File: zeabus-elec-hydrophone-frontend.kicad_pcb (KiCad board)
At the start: 4 copper layers, 53.3 x 68.6 mm, 153 parts, among them CN1 EPS.00.250.NTN, CN2 EPS.00.250.NTN, CN3 EPS.00.250.NTN, CN4 EPS.00.250.NTN, J1 Conn_R1, J10 TEST_1P, J11 TEST_1P, J12 TEST_1P, J13 TEST_1P, J14 TEST_1P, J15 TEST_1P, J16 TEST_1P, J17 TEST_1P, J18 TEST_1P, J2 Conn_L1, J3 Conn_R2, J4 Conn_L2, J5 TEST_1P, J6 TEST_1P, J7 TEST_1P, J8 TEST_1P, J9 TEST_1P, U1 AD8334ACPZ, U2 TLV73311PDBVT, U3 MAX5387LAUD+T, U4 OPA2365, U5 OPA2365

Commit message: First released
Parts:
- added REF**: 1pin, Connectors:1pin, F.Cu at (175.4, 78.9)
- added REF**: 1pin, Connectors:1pin, F.Cu at (129.9, 79.0)
- C39, C40, C41, C42, C43, C44, C45, C46, C47, C49, C50, C51, C52, C53, C54, R21, R22, R23, R24, R25, R26, R27, R28, R29, R30, R31, R32, R33, R34, R35, R36, R37, R38, R39, R40, R41, R42, R43, R44, R45, R46, R47, R48, R49, R50, U4, U5: moved to B.Cu
- C48: footprint Capacitors_SMD:C_1206_HandSoldering -> Capacitors_SMD:C_1210_HandSoldering; moved to B.Cu
- moved C50 78.2 mm to (169.5, 97.5), turned to 180 degrees
- moved C26 74.1 mm to (164.5, 94.0), turned to 180 degrees
- moved C52 73.6 mm to (165.0, 109.5), turned to 180 degrees
- moved L20 71.1 mm to (159.0, 84.6)
- moved C38 68.6 mm to (162.6, 100.9), turned to 90 degrees
- moved C54 68.2 mm to (165.2, 97.5)
- moved C27 67.0 mm to (159.6, 125.9)
- moved C25 65.9 mm to (164.1, 100.8), turned to 90 degrees
- moved L13 65.6 mm to (159.0, 87.9)
- moved C37 64.4 mm to (164.1, 105.2), turned to 270 degrees
- moved C36 63.5 mm to (171.3, 124.3), turned to 180 degrees
- moved C42 63.4 mm to (165.0, 107.8), turned to 180 degrees
- moved L16 63.1 mm to (144.3, 91.1), turned to 180 degrees
- moved L17 63.1 mm to (154.2, 84.6)
- moved C35 63.1 mm to (171.3, 125.9)
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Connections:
- U2 pad 1: +3.3VA -> +3V3
- U2 pad 3: +3.3VA -> +3V3
- U4 pad 5: Net-(R22-Pad1) -> Net-(R37-Pad1)
- U4 pad 6: Net-(R32-Pad1) -> Net-(R47-Pad1)
- U4 pad 7: Net-(R28-Pad2) -> Net-(R43-Pad2)
- U5 pad 1: Net-(R43-Pad2) -> Net-(R28-Pad2)
- U5 pad 2: Net-(R47-Pad1) -> Net-(R32-Pad1)
- U5 pad 3: Net-(R37-Pad1) -> Net-(R22-Pad1)
- U5 pad 4: Net-(U5-Pad4) -> GNDA
- U5 pad 8: Net-(U5-Pad8) -> +3V3
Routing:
- net +3V3: track 0.00 -> 94.6 mm, vias 0 -> 1
- net VA_REF: track 0.00 -> 72.8 mm
- net /ADC3: track 0.00 -> 49.8 mm
- net +5V: track 0.00 -> 43.0 mm, vias 0 -> 7
- net /LNA Gain Control/GAIN12: track 0.00 -> 42.8 mm, vias 0 -> 2
- net /LNA/LNA1RN: track 0.00 -> 41.5 mm
- net /ADC2: track 0.00 -> 40.0 mm
- net /LNA/LNA2RP: track 0.00 -> 39.7 mm
- net /ADC0: track 0.00 -> 35.0 mm
- net /ADC1: track 0.00 -> 33.7 mm
- net /LNA/INH3: track 0.00 -> 33.5 mm
- net /LNA/INH4: track 0.00 -> 33.1 mm
- net /LNA/LNA2LN: track 0.00 -> 32.9 mm
- net /LNA/LNA1LN: track 0.00 -> 32.2 mm
- net /LNA/LNA1LP: track 0.00 -> 30.1 mm
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- added copper zone on In2.Cu, net +5V
- added copper zone on B.Cu, net GNDA
- added copper zone on F.Cu, net GNDA
- added copper zone on In1.Cu, net GNDA
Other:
- net class Default: clearance 0.2 -> 0.127; trace_width 0.25 -> 0.127; via_dia 0.6 -> 0.5588; via_drill 0.4 -> 0.3048
- rule trace_clearance: 0.2 -> 0.127
- rule trace_min: 0.2 -> 0.127
- rule via_min_drill: 0.3 -> 0.3048
- rule via_min_size: 0.4 -> 0.5588

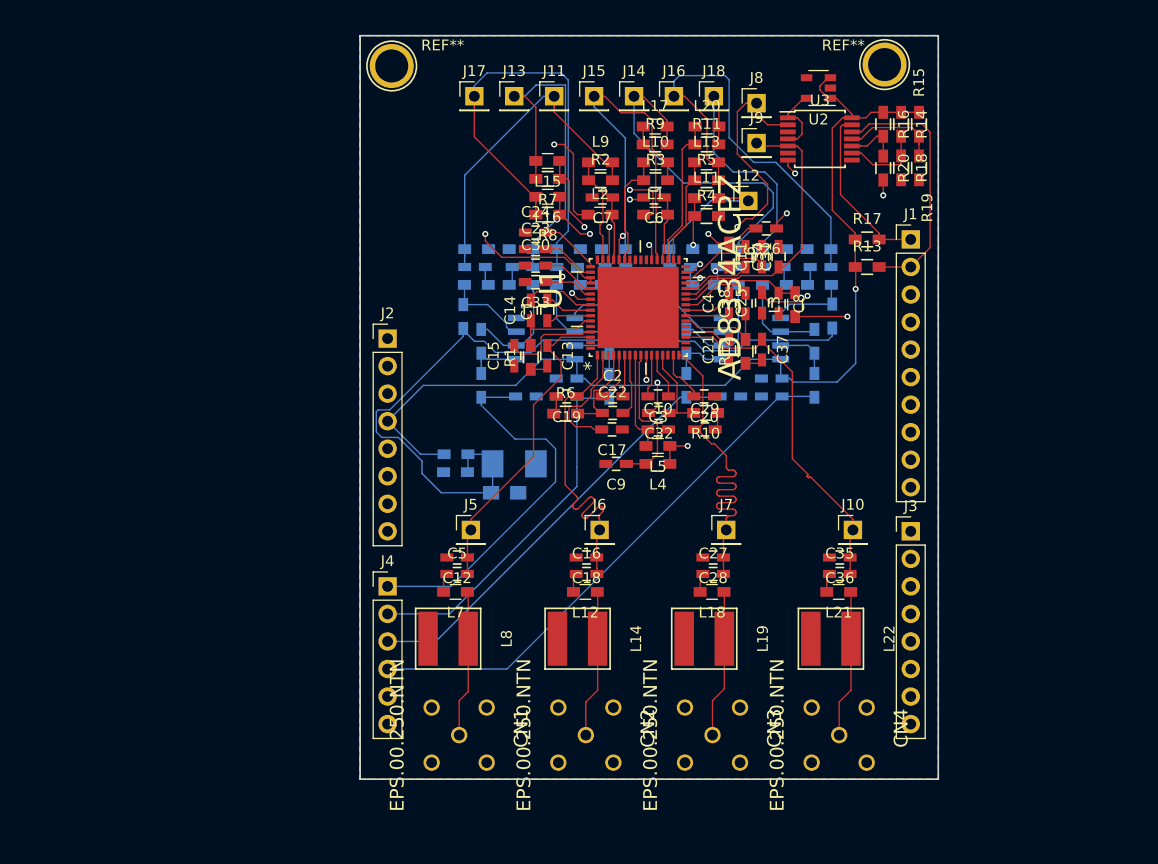
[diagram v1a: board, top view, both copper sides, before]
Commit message: edit layout and silkscreen
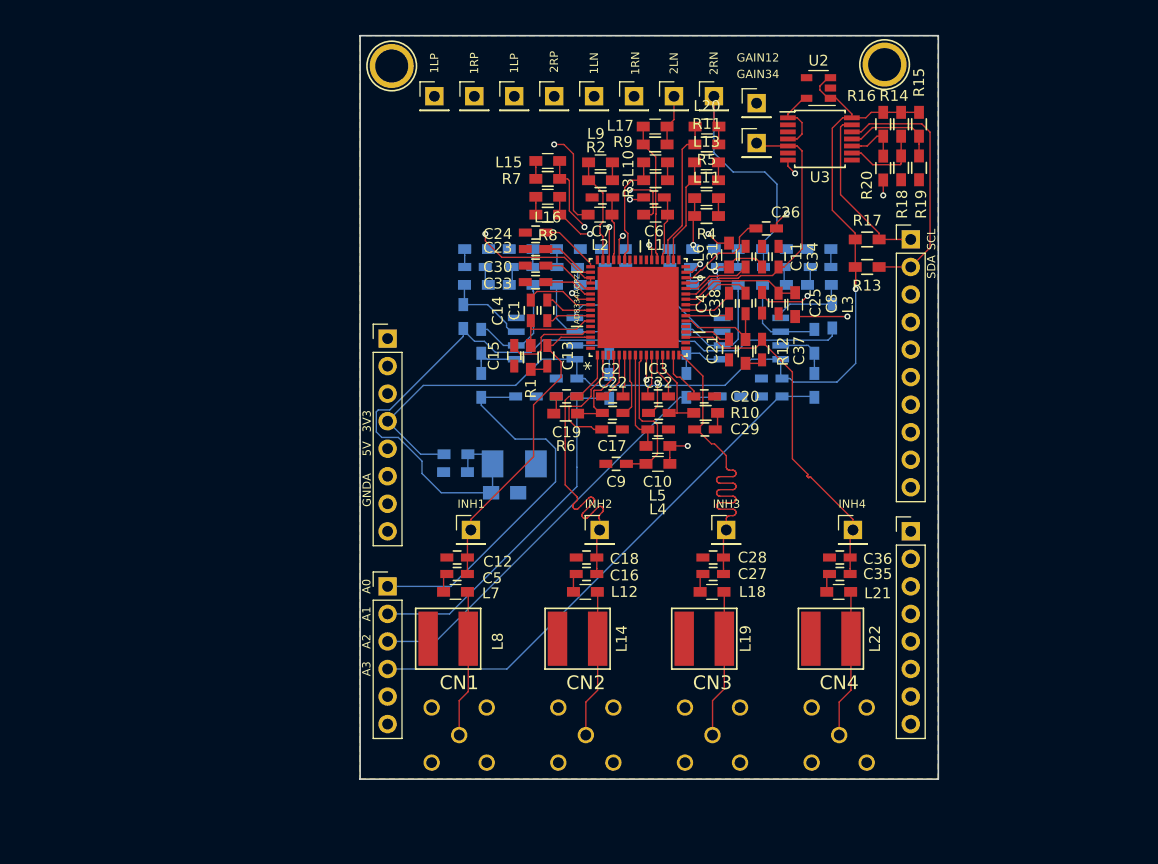
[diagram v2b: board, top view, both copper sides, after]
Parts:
- moved J12 23.6 mm to (141.2, 81.8)
- moved J17 14.7 mm to (152.3, 81.8)
- moved J11 11.0 mm to (133.9, 81.8)
- moved J15 11.0 mm to (137.5, 81.8)
- moved J16 11.0 mm to (144.9, 81.8)
- moved J13 7.37 mm to (148.6, 81.8)
- moved J14 3.68 mm to (156.0, 81.8)
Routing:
- net /LNA Gain Control/GAIN12: track 42.8 -> 4.58 mm, vias 2 -> 0
- net /LNA/LNA1RN: track 41.5 -> 3.47 mm
- net /LNA/LNA2RP: track 39.7 -> 3.30 mm
- net /LNA/LNA1LN: track 32.2 -> 3.31 mm
- net /LNA/LNA1LP: track 30.1 -> 3.30 mm
- net /LNA/LNA2LN: track 32.9 -> 6.37 mm
- net /LNA/LNA1RP: track 29.5 -> 3.47 mm
- net /LNA/LNA2LP: track 15.7 -> 3.34 mm
- net /LNA/LNA2RN: track 25.1 -> 25.8 mm
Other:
- board text added: "1LN"
- board text added: "1LP"
- board text added: "1RN"
- board text added: "1RP"
- board text added: "2LN"
- board text added: "2RN"
- board text added: "2RP"
- board text added: "3V3"
- board text added: "5V"
- board text added: "A0"
- board text added: "A1"
- board text added: "A2"
- board text added: "A3"
- board text added: "GAIN12"
- board text added: "GAIN34"
- board text added: "GNDA"
- board text added: "INH1"
- board text added: "INH2"
- board text added: "INH3"
- board text added: "INH4"
- board text added: "SCL"
- board text added: "SDA"

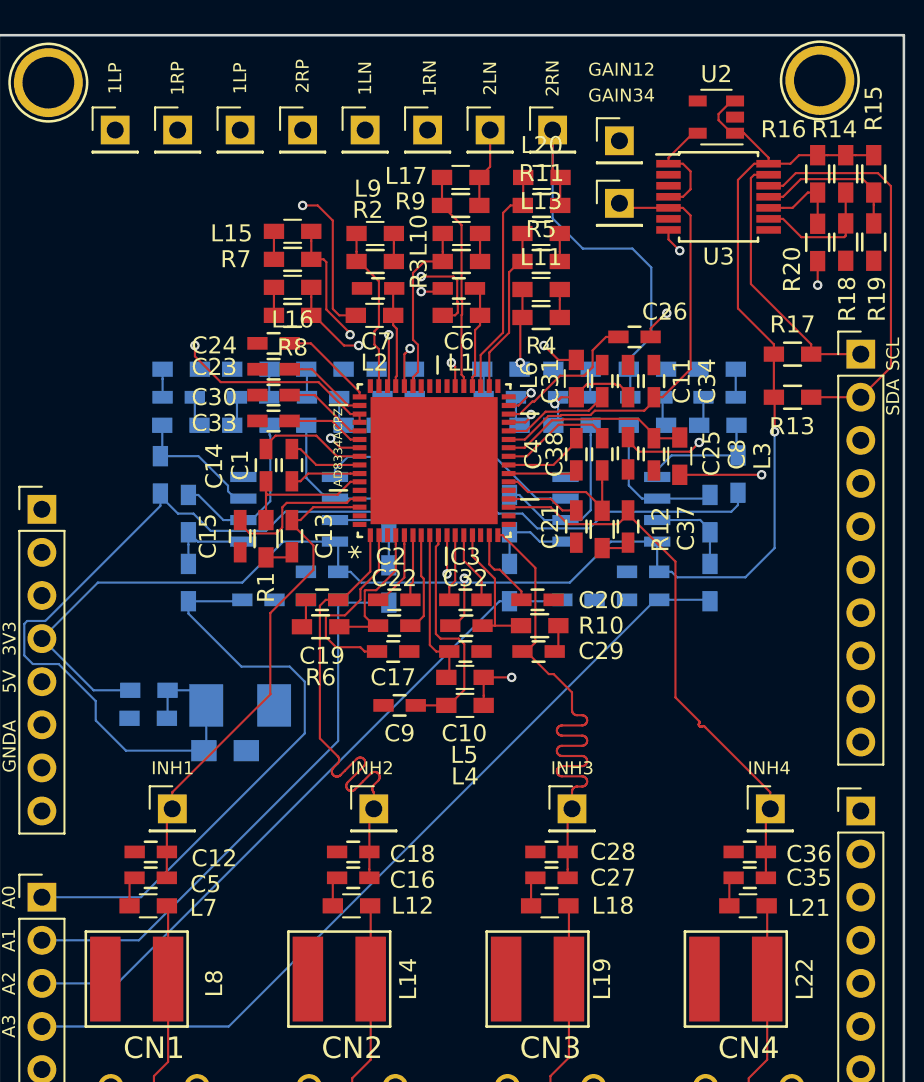
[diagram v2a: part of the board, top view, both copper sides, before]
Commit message: Finished the PCB plus adding some stitching vias
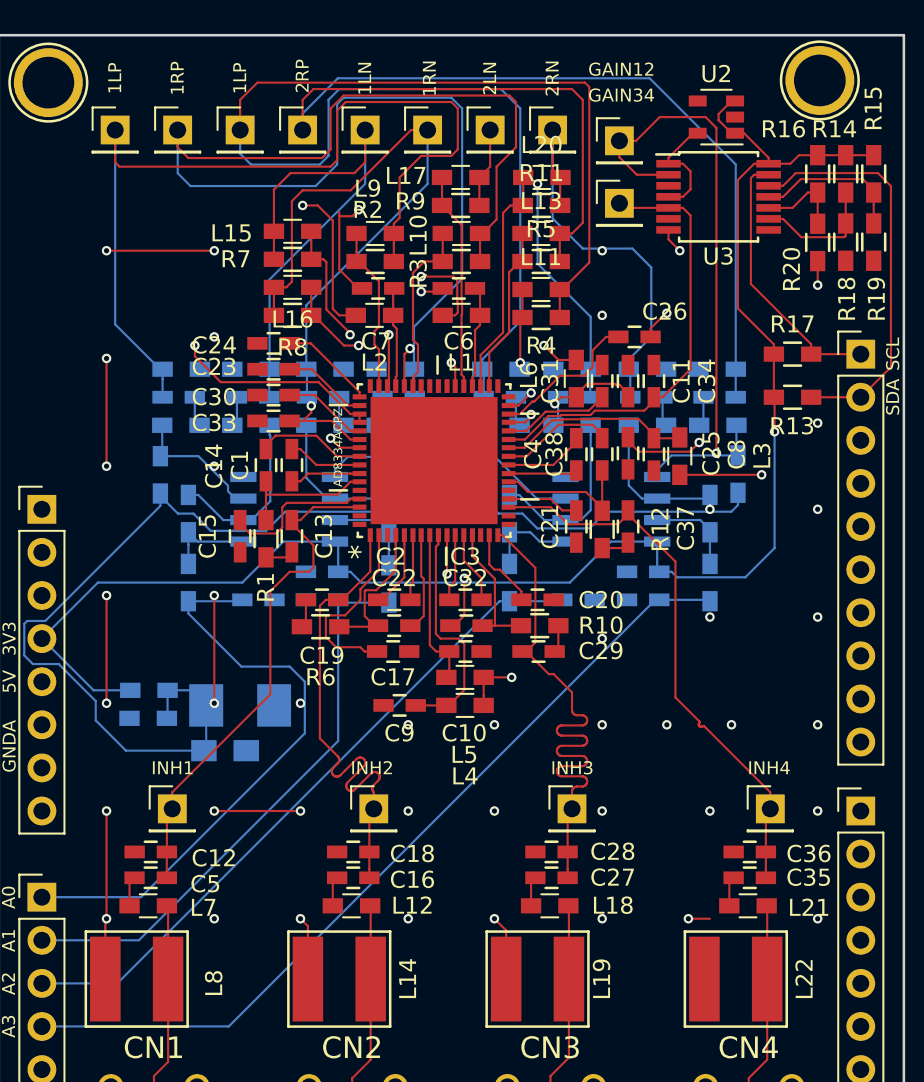
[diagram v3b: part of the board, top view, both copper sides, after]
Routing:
- net GNDA: track 6.10 -> 100.0 mm, vias 4 -> 19
- net /LNA/LNA2LP: track 3.34 -> 77.7 mm
- net /LNA/LNA1RP: track 3.47 -> 77.2 mm
- net /LNA/LNA2RP: track 3.30 -> 72.5 mm
- net /LNA Gain Control/GAIN12: track 4.58 -> 63.5 mm, vias 0 -> 2
- net /LNA/LNA1LP: track 3.30 -> 54.4 mm
- net /LNA/LNA1RN: track 3.47 -> 36.2 mm
- net /LNA/LNA1LN: track 3.31 -> 30.1 mm
- net /LNA/LNA2LN: track 6.37 -> 22.9 mm, vias 0 -> 1
- net (no net): track 0.00 -> 6.35 mm, vias 0 -> 27
- net /LNA/INH1: track 29.5 -> 30.2 mm

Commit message: add gerber file and sent to pcbway
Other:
- board text added: "ZEABUS Hydrophone Sensor Front End REV 1.0"
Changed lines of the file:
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@@
     (links 291)
     (no_connects 0)
-    (area 126.293952 76.124999 181.141286 154.876501)
+    (area 126.293952 68.547 190.273715 154.876501)
     (thickness 1.6)
-    (drawings 27)
+    (drawings 30)
     (tracks 1128)
     (zones 0)
@@
     (visible_elements 7FFFFFFF)
     (pcbplotparams
-      (layerselection 0x00030_80000001)
-      (usegerberextensions false)
+      (layerselection 0x030fc_80000007)
+      (usegerberextensions true)
       (excludeedgelayer true)
       (linewidth 0.100000)
@@
       (plotinvisibletext false)
       (padsonsilk false)
-      (subtractmaskfromsilk false)
+      (subtractmaskfromsilk true)
       (outputformat 1)
       (mirror false)
-      (drillshape 1)
+      (drillshape 0)
       (scaleselection 1)
-      (outputdirectory ""))
+      (outputdirectory plot/))
   )
   (net 0 "")
@@
       (net 12 GNDA))
   )
+  (gr_text "ZEABUS Hydrophone \nSensor Front End \nREV 1.0" (at 130.302 93.091 270) (layer F.SilkS)
+    (effects (font (size 0.762 0.762) (thickness 0.127)))
+  )
+  (dimension 68.58 (width 0.3) (layer Margin)
+    (gr_text "2.7000 in" (at 184.738 110.49 270) (layer Margin)
+      (effects (font (size 1.5 1.5) (thickness 0.3)))
+    )
+    (feature1 (pts (xy 180.34 144.78) (xy 186.088 144.78)))
+    (feature2 (pts (xy 180.34 76.2) (xy 186.088 76.2)))
+    (crossbar (pts (xy 183.388 76.2) (xy 183.388 144.78)))
+    (arrow1a (pts (xy 183.388 144.78) (xy 182.801579 143.653496)))
+    (arrow1b (pts (xy 183.388 144.78) (xy 183.974421 143.653496)))
+    (arrow2a (pts (xy 183.388 76.2) (xy 182.801579 77.326504)))
+    (arrow2b (pts (xy 183.388 76.2) (xy 183.974421 77.326504)))
+  )
+  (dimension 53.34 (width 0.3) (layer Margin)
+    (gr_text "2.1000 in" (at 153.67 69.897) (layer Margin)
+      (effects (font (size 1.5 1.5) (thickness 0.3)))
+    )
+    (feature1 (pts (xy 180.34 76.2) (xy 180.34 68.547)))
+    (feature2 (pts (xy 127 76.2) (xy 127 68.547)))
+    (crossbar (pts (xy 127 71.247) (xy 180.34 71.247)))
+    (arrow1a (pts (xy 180.34 71.247) (xy 179.213496 71.833421)))
+    (arrow1b (pts (xy 180.34 71.247) (xy 179.213496 70.660579)))
+    (arrow2a (pts (xy 127 71.247) (xy 128.126504 71.833421)))
+    (arrow2b (pts (xy 127 71.247) (xy 128.126504 70.660579)))
+  )
   (gr_text 1LP (at 141.224 78.74 90) (layer F.SilkS)
     (effects (font (size 0.762 0.762) (thickness 0.127)))
@@
     (effects (font (size 0.762 0.762) (thickness 0.127)))
   )
-  (gr_text A3 (at 127.6 134.6 90) (layer F.SilkS)
+  (gr_text A3 (at 127.6 134.6 270) (layer F.SilkS)
     (effects (font (size 0.762 0.762) (thickness 0.127)))
   )
-  (gr_text A2 (at 127.6 132.08 90) (layer F.SilkS)
+  (gr_text A2 (at 127.6 132.08 270) (layer F.SilkS)
     (effects (font (size 0.762 0.762) (thickness 0.127)))
   )
-  (gr_text A1 (at 127.6 129.54 90) (layer F.SilkS)
+  (gr_text A1 (at 127.6 129.54 270) (layer F.SilkS)
     (effects (font (size 0.762 0.762) (thickness 0.127)))
   )
-  (gr_text A0 (at 127.6 127 90) (layer F.SilkS)
+  (gr_text A0 (at 127.6 127 270) (layer F.SilkS)
     (effects (font (size 0.762 0.762) (thickness 0.127)))
   )
-  (gr_text GNDA (at 127.635 118.11 90) (layer F.SilkS)
+  (gr_text GNDA (at 127.635 118.11 270) (layer F.SilkS)
     (effects (font (size 0.762 0.762) (thickness 0.127)))
   )
-  (gr_text 5V (at 127.635 114.3 90) (layer F.SilkS)
+  (gr_text 5V (at 127.635 114.3 270) (layer F.SilkS)
     (effects (font (size 0.762 0.762) (thickness 0.127)))
   )
-  (gr_text 3V3 (at 127.635 111.76 90) (layer F.SilkS)
+  (gr_text 3V3 (at 127.635 111.76 270) (layer F.SilkS)
     (effects (font (size 0.762 0.762) (thickness 0.127)))
   )
